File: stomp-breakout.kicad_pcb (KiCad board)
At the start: 2 copper layers, 24.3 x 21.2 mm, 9 parts, among them J1 Stomp_Connector, J2 JO, J3 JI, J4 Power_SIDE, J5 Power_TOP

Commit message: v0.2: board input grounded in bypass
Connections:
- S1 pad 1: IN -> JACK_IN
- S1 pad 2: JACK_IN -> IN
- S1 pad 4: GND -> LED-
- S1 pad 5: LED- -> GND
- S1 pad 6: Net-(S1-Pad6) -> Net-(S1-Pad3)
- S1 pad 9: Net-(S1-Pad3) -> JACK_IN
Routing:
- net JACK_IN: track 6.96 -> 31.5 mm
- net Net-(S1-Pad3): track 12.6 -> 5.30 mm
- net LED-: track 32.6 -> 26.4 mm
- net Net-(D1-Pad2): track 10.2 -> 15.8 mm
- net IN: track 6.84 -> 12.3 mm
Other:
- board text added: "v0.2 2020-03-27"
- board text removed: "v0.1 2020-03-14"

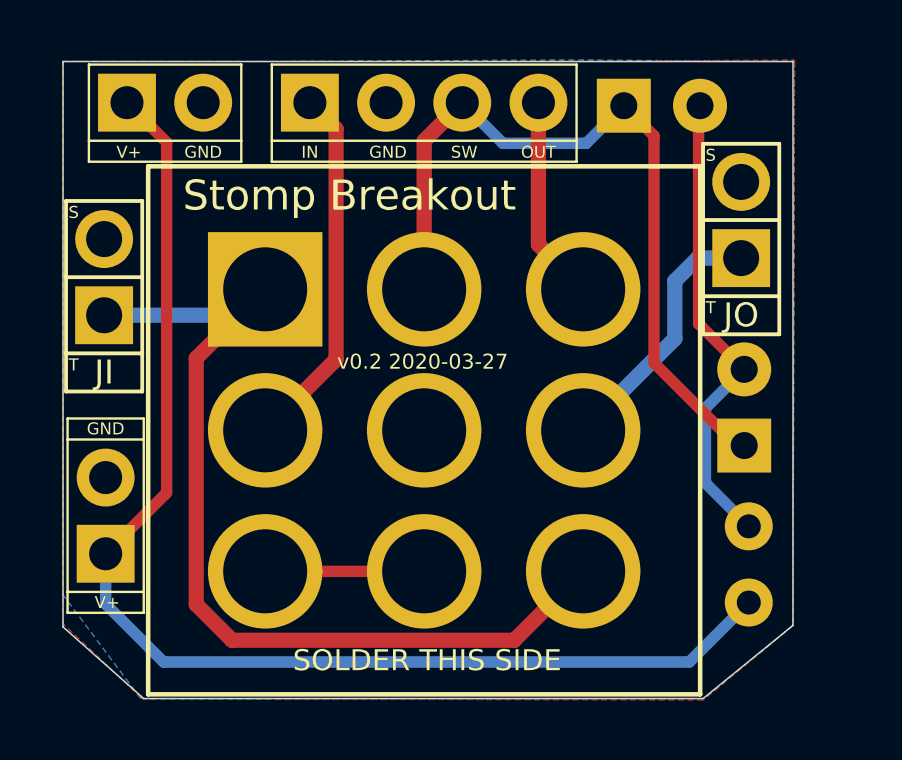
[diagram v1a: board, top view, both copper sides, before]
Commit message: v0.4: optional bicolor CA LED, anti-pop capacitor & resistor
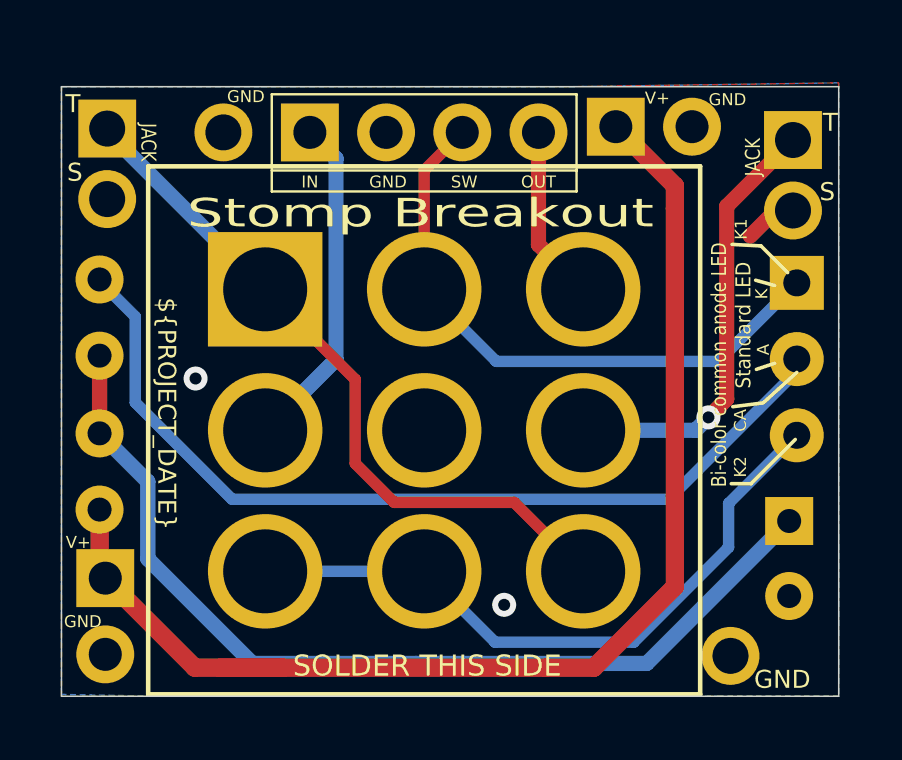
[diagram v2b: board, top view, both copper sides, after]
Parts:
- removed D2: LED, LED_THT:LED_D3.0mm
- added C1: 10u, rockola_kicad_footprints:CP_D5.0_P2.50, B.Cu at (159.9, 97.7)
- added J6: GND, rockola_kicad_footprints:1PAD, F.Cu at (139.8, 84.7)
- added J7: GND, rockola_kicad_footprints:1PAD, F.Cu at (156.7, 102.2)
- added R2: 390R, rockola_kicad_footprints:Resistor_0.25W_Standing, B.Cu at (136.9, 89.6)
- D1: value LED -> LED_Dual_CAC; footprint LED_THT:LED_D3.0mm -> LED_THT:LED_D5.0mm-3
- J2: value JO -> OUT; footprint rockola_kicad_footprints:2PADS_TS_Horizontal -> rockola_kicad_footprints:2PADS_TS_Vertical_NOBORDER
- J3: value JI -> IN; footprint rockola_kicad_footprints:2PADS_TS_Horizontal -> rockola_kicad_footprints:2PADS_TS_Vertical_NOBORDER
- J4: footprint rockola_kicad_footprints:Power_Header_2pin_VERTICAL_ALT -> rockola_kicad_footprints:Power_Header_2pin_VERTICAL_ALT_NOBORDER
- J5: footprint rockola_kicad_footprints:Power_Header_2pin_TOP_ALT -> rockola_kicad_footprints:Power_Header_2pin_TOP_ALT_NOBORDER
- moved R1 21.9 mm to (136.9, 94.7)
- moved J5 16.3 mm to (157.9, 84.5)
- moved D1 5.70 mm to (160.1, 89.7), turned to -90 degrees
- moved J4 4.21 mm to (135.8, 100.8), turned to 180 degrees
- moved J3 3.81 mm to (137.2, 85.7), turned to 0 degrees
- moved J2 2.30 mm to (160.0, 86.1), turned to 0 degrees
- moved J1 0.99 mm to (147.7, 84.7)
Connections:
- D1 pad 2: Net-(D1-Pad2) -> Net-(D2-Pad2)
- R1 pad 1: Net-(D1-Pad2) -> Net-(C1-Pad1)
- S1 pad 3: Net-(S1-Pad3) -> LED2-
- S1 pad 6: Net-(S1-Pad3) -> LED2-
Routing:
- net Net-(C1-Pad1): track 0.00 -> 32.5 mm
- net Net-(D2-Pad2): track 0.00 -> 30.1 mm
- net LED2-: track 0.00 -> 22.4 mm
- net Net-(D1-Pad2): track 15.8 -> 0.00 mm
- net JACK_IN: track 31.5 -> 23.7 mm
- net LED-: track 26.4 -> 20.3 mm
- net JACK_OUT: track 8.77 -> 14.8 mm, vias 0 -> 1
- net Net-(S1-Pad3): track 5.30 -> 0.00 mm
- net GND: track 0.00 -> 2.26 mm, vias 0 -> 2
- net OUT: track 6.84 -> 5.85 mm
- net IN: track 12.3 -> 11.3 mm
- net +9V: track 41.2 -> 42.0 mm
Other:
- board size 24.3 x 21.2 mm -> 25.9 x 20.3 mm
- board text added: "${REVISION} ${PROJECT_DATE}"
- board text added: "A"
- board text added: "Bi-color common anode LED"
- board text added: "CA"
- board text added: "GND"
- board text added: "JACK"
- board text added: "K1"
- board text added: "K2"
- board text added: "LED"
- board text added: "Standard LED"
- board text removed: "v0.2 2020-03-27"

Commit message: updated to KiCad 6.0
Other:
- net class Default removed
